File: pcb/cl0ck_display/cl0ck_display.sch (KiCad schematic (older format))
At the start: 12 parts, among them P1 CONN_01X03, P2 CONN_01X02

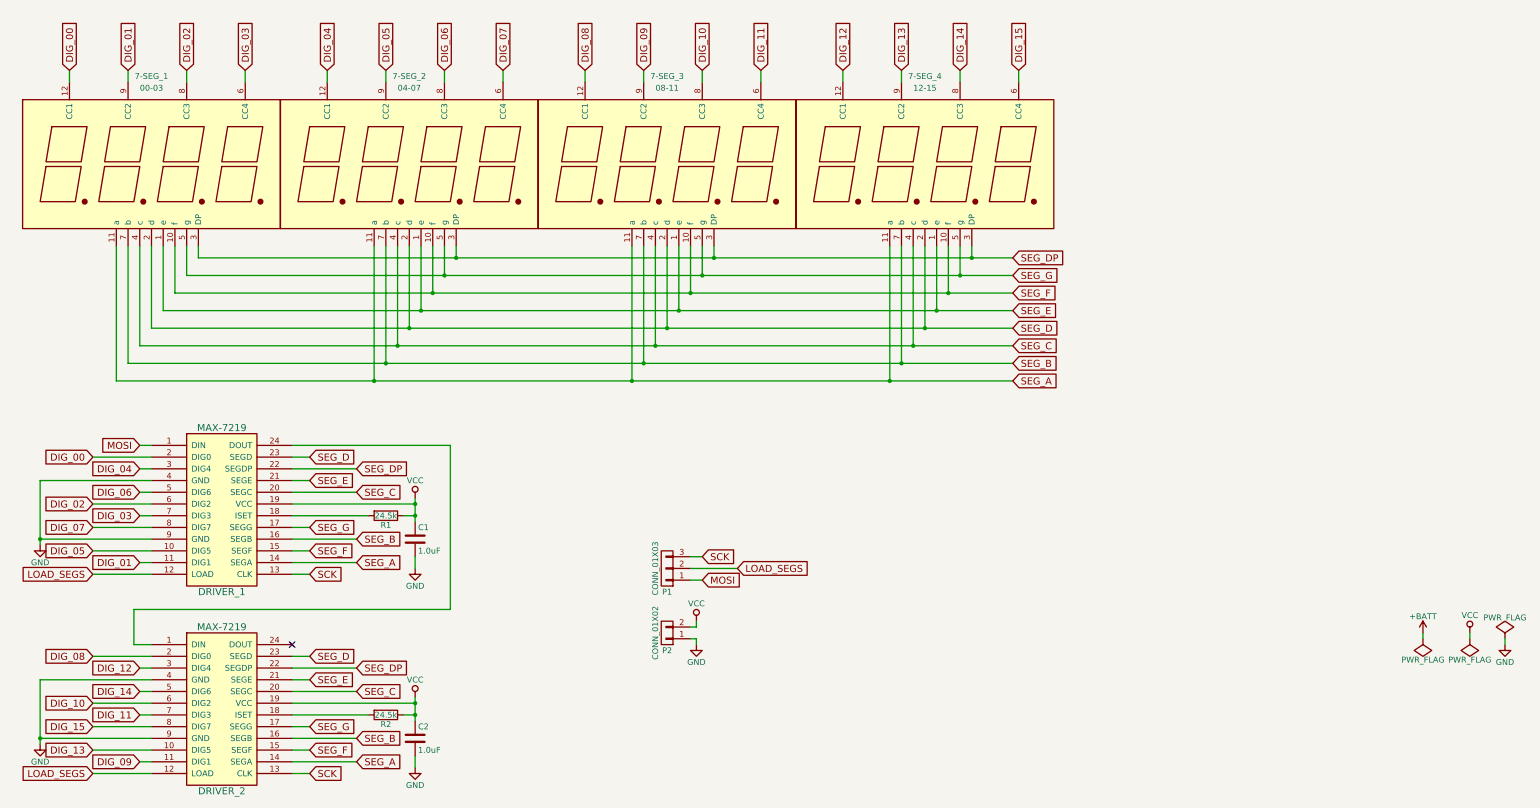
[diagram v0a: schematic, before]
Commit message: Created display PCB from schematic.
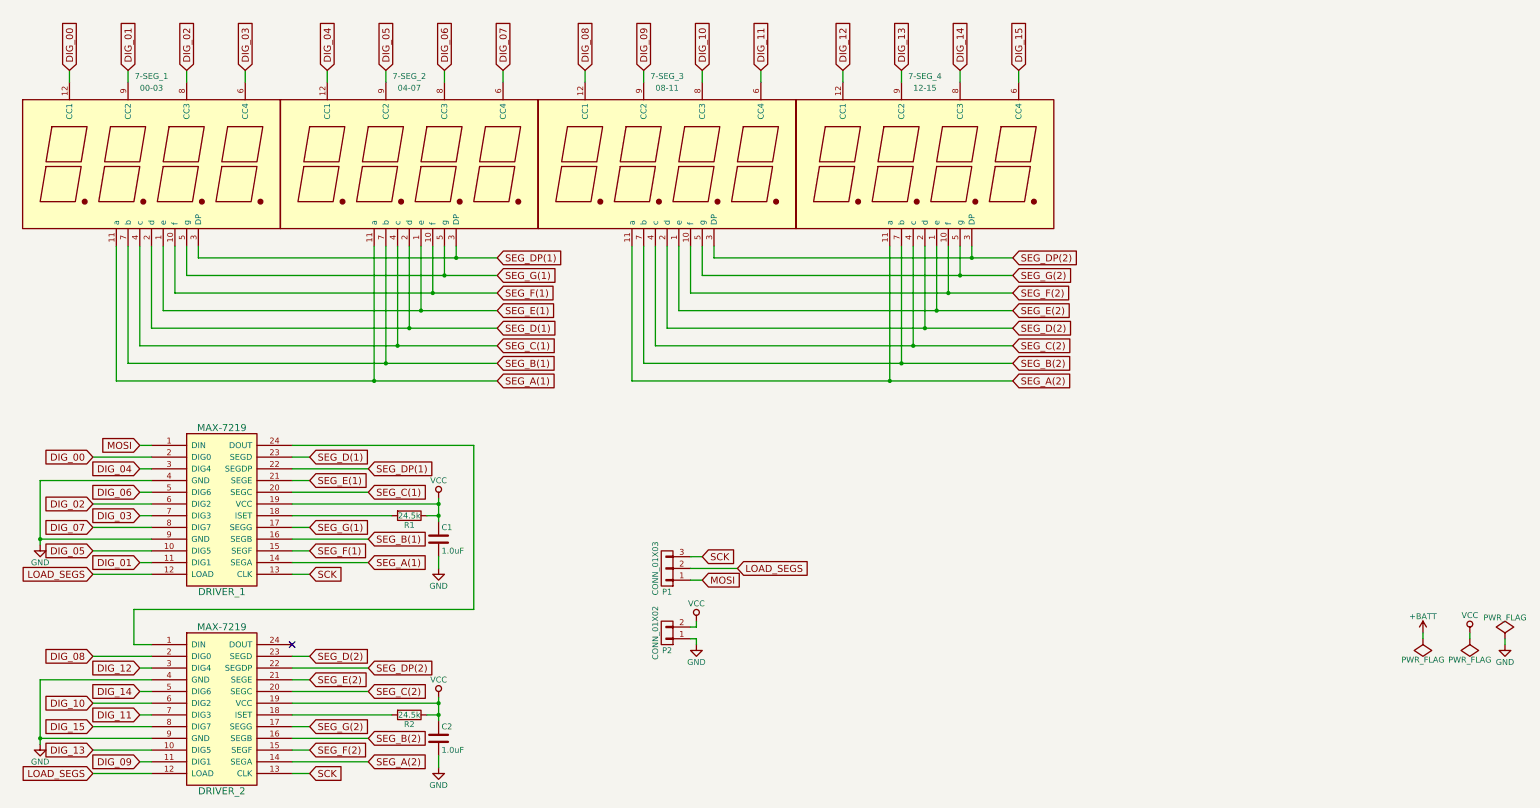
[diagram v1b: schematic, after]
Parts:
- 7-SEG_1, 7-SEG_2, 7-SEG_3, 7-SEG_4: footprint Displays_7-Segment:Cx56-12 -> cl0ck_display:4x7-SEG
- DRIVER_1, DRIVER_2: footprint (none) -> Housings_SOIC:SOIC-24W_7.5x15.4mm_Pitch1.27mm
- P1: footprint (none) -> Pin_Headers:Pin_Header_Straight_1x03
- P2: footprint (none) -> Pin_Headers:Pin_Header_Straight_1x02
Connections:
- net SEG_A renamed SEG_A(1)
- net SEG_A(1): no longer 7-SEG_3.11 (a), 7-SEG_4.11 (a), DRIVER_2.14 (SEGA)
- net SEG_B renamed SEG_B(1)
- net SEG_B(1): no longer 7-SEG_3.7 (b), 7-SEG_4.7 (b), DRIVER_2.16 (SEGB)
- net SEG_C renamed SEG_C(1)
- net SEG_C(1): no longer 7-SEG_3.4 (c), 7-SEG_4.4 (c), DRIVER_2.20 (SEGC)
- net SEG_D renamed SEG_D(1)
- net SEG_D(1): no longer 7-SEG_3.2 (d), 7-SEG_4.2 (d), DRIVER_2.23 (SEGD)
- net SEG_DP renamed SEG_DP(1)
- net SEG_DP(1): no longer 7-SEG_3.3 (DP), 7-SEG_4.3 (DP), DRIVER_2.22 (SEGDP)
- net SEG_E renamed SEG_E(1)
- net SEG_E(1): no longer 7-SEG_3.1 (e), 7-SEG_4.1 (e), DRIVER_2.21 (SEGE)
- net SEG_F renamed SEG_F(1)
- net SEG_F(1): no longer 7-SEG_3.10 (f), 7-SEG_4.10 (f), DRIVER_2.15 (SEGF)
- net SEG_G renamed SEG_G(1)
- net SEG_G(1): no longer 7-SEG_3.5 (g), 7-SEG_4.5 (g), DRIVER_2.17 (SEGG)
- new net SEG_A(2): 7-SEG_3.11 (a), 7-SEG_4.11 (a), DRIVER_2.14 (SEGA)
- new net SEG_B(2): 7-SEG_3.7 (b), 7-SEG_4.7 (b), DRIVER_2.16 (SEGB)
- new net SEG_C(2): 7-SEG_3.4 (c), 7-SEG_4.4 (c), DRIVER_2.20 (SEGC)
- new net SEG_D(2): 7-SEG_3.2 (d), 7-SEG_4.2 (d), DRIVER_2.23 (SEGD)
- new net SEG_DP(2): 7-SEG_3.3 (DP), 7-SEG_4.3 (DP), DRIVER_2.22 (SEGDP)
- new net SEG_E(2): 7-SEG_3.1 (e), 7-SEG_4.1 (e), DRIVER_2.21 (SEGE)
- new net SEG_F(2): 7-SEG_3.10 (f), 7-SEG_4.10 (f), DRIVER_2.15 (SEGF)
- new net SEG_G(2): 7-SEG_3.5 (g), 7-SEG_4.5 (g), DRIVER_2.17 (SEGG)
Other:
- moved on the sheet: C1, C2, R1, R2
